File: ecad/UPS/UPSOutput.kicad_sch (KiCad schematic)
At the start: 29 parts, among them J3 USB_C_Receptacle_USB2.0_16P, Q3 IRLR7843TRPBF, SW3 SW_DPDT_x2, U2 MPQ5031GRE-0001-AEC1-P

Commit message: Swapped 201 resistor footprint
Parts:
- R40: footprint Resistor_SMD:R_0201_0603Metric_Pad0.64x0.40mm_HandSolder -> Resistor_SMD:R_0603_1608Metric_Pad0.98x0.95mm_HandSolder
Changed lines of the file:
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@@
 			)
 		)
-		(property "Footprint" "Resistor_SMD:R_0201_0603Metric_Pad0.64x0.40mm_HandSolder"
+		(property "Footprint" "Resistor_SMD:R_0603_1608Metric_Pad0.98x0.95mm_HandSolder"
 			(at 159.512 29.21 90)
 			(hide yes)

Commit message: Update R41 Resistor from 0201 to 0603
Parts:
- R41: footprint Resistor_SMD:R_0201_0603Metric_Pad0.64x0.40mm_HandSolder -> Resistor_SMD:R_0603_1608Metric_Pad0.98x0.95mm_HandSolder
- renumbered C9 to C?, C6 to C?, C10 to C?, C11 to C?, C5 to C?, C12 to C?, D4 to D?, D3 to D?, D5 to D?, D1 to D?, D2 to D?, J3 to J1, R7 to R?, R6 to R?, R8 to R?, TH1 to TH?, U2 to U1
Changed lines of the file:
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@@
 		(dnp no)
 		(fields_autoplaced yes)
-		(property "Reference" "#PWR0102"
+		(property "Reference" "#PWR03"
 			(at 66.04 33.02 0)
 			(hide yes)
@@
 		)
 		(instances
-			(project ""
+			(project "UPSOutput"
 				(path "/917f3576-2b89-40c4-9175-933056884ccc"
 					(reference "#PWR03")
@@
 		(in_pos_files yes)
 		(dnp no)
-		(property "Reference" "R7"
+		(property "Reference" "R?"
 			(at 142.24 50.292 90)
 			(show_name no)
@@
 		)
 		(instances
+			(project "UPSOutput"
+				(path "/917f3576-2b89-40c4-9175-933056884ccc"
+					(reference "TP6")
+					(unit 1)
+				)
+			)
 			(project "UPS"
 				(path "/9d92b60a-4a6b-449c-b462-cab19e69d38c/c2035c51-7de6-43a1-947f-d073f8318def"
@@
 		(in_pos_files yes)
 		(dnp no)
-		(property "Reference" "D4"
+		(property "Reference" "D?"
 			(at 195.58 76.2001 90)
 			(show_name no)
@@
 		)
 		(instances
+			(project "UPSOutput"
+				(path "/917f3576-2b89-40c4-9175-933056884ccc"
+					(reference "#PWR051")
+					(unit 1)
+				)
+			)
 			(project "UPS"
 				(path "/9d92b60a-4a6b-449c-b462-cab19e69d38c/c2035c51-7de6-43a1-947f-d073f8318def"
@@
 		(dnp no)
 		(fields_autoplaced yes)
-		(property "Reference" "#PWR09"
+		(property "Reference" "#PWR?"
 			(at 182.88 91.44 0)
 			(hide yes)
@@
 		(in_pos_files yes)
 		(dnp no)
-		(property "Reference" "D3"
+		(property "Reference" "D?"
 			(at 185.42 76.2001 90)
 			(show_name no)
@@
 		(in_pos_files yes)
 		(dnp no)
-		(property "Reference" "R6"
+		(property "Reference" "R?"
 			(at 142.24 43.688 90)
 			(show_name no)
@@
 		)
 		(instances
+			(project "UPSOutput"
+				(path "/917f3576-2b89-40c4-9175-933056884ccc"
+					(reference "C59")
+					(unit 1)
+				)
+			)
 			(project "UPS"
 				(path "/9d92b60a-4a6b-449c-b462-cab19e69d38c/c2035c51-7de6-43a1-947f-d073f8318def"
@@
 		(dnp no)
 		(fields_autoplaced yes)
-		(property "Reference" "C9"
+		(property "Reference" "C?"
 			(at 68.58 73.6599 0)
 			(show_name no)
@@
 		(in_pos_files yes)
 		(dnp no)
-		(property "Reference" "U2"
+		(property "Reference" "U1"
 			(at 92.71 74.93 0)
 			(show_name no)
@@
 		)
 		(instances
-			(project ""
+			(project "UPSOutput"
 				(path "/917f3576-2b89-40c4-9175-933056884ccc"
 					(reference "U1")
@@
 			)
 		)
-		(property "Footprint" "Resistor_SMD:R_0201_0603Metric_Pad0.64x0.40mm_HandSolder"
+		(property "Footprint" "Resistor_SMD:R_0603_1608Metric_Pad0.98x0.95mm_HandSolder"
 			(at 159.512 39.37 90)
 			(hide yes)
@@
 		)
 		(instances
+			(project "UPSOutput"
+				(path "/917f3576-2b89-40c4-9175-933056884ccc"
+					(reference "R41")
+					(unit 1)
+				)
+			)
 			(project "UPS"
 				(path "/9d92b60a-4a6b-449c-b462-cab19e69d38c/c2035c51-7de6-43a1-947f-d073f8318def"
@@
 		)
 		(instances
+			(project "UPSOutput"
+				(path "/917f3576-2b89-40c4-9175-933056884ccc"
+					(reference "C64")
+					(unit 1)
+				)
+			)
 			(project "UPS"
 				(path "/9d92b60a-4a6b-449c-b462-cab19e69d38c/c2035c51-7de6-43a1-947f-d073f8318def"
@@
 		)
 		(instances
+			(project "UPSOutput"
+				(path "/917f3576-2b89-40c4-9175-933056884ccc"
+					(reference "TP7")
+					(unit 1)
+				)
+			)
 			(project "UPS"
 				(path "/9d92b60a-4a6b-449c-b462-cab19e69d38c/c2035c51-7de6-43a1-947f-d073f8318def"
@@
 		(dnp no)
 		(fields_autoplaced yes)
-		(property "Reference" "#PWR010"
+		(property "Reference" "#PWR?"
 			(at 198.12 91.44 0)
 			(hide yes)
@@
 		(in_pos_files yes)
 		(dnp no)
-		(property "Reference" "C6"
+		(property "Reference" "C?"
 			(at 123.19 68.834 0)
 			(show_name no)
@@
 		(dnp no)
 		(fields_autoplaced yes)
-		(property "Reference" "#PWR0104"
+		(property "Reference" "#PWR01"
 			(at 243.84 21.59 0)
 			(hide yes)
@@
 		)
 		(instances
-			(project ""
+			(project "UPSOutput"
 				(path "/917f3576-2b89-40c4-9175-933056884ccc"
 					(reference "#PWR01")
@@
 		(dnp no)
 		(fields_autoplaced yes)
-		(property "Reference" "#PWR0108"
+		(property "Reference" "#PWR?"
 			(at 58.42 133.35 0)
 			(hide yes)
@@
 		(dnp no)
 		(fields_autoplaced yes)
-		(property "Reference" "#PWR011"
+		(property "Reference" "#PWR?"
 			(at 113.03 25.4 0)
 			(hide yes)
@@
 		)
 		(instances
+			(project "UPSOutput"
+				(path "/917f3576-2b89-40c4-9175-933056884ccc"
+					(reference "Q3")
+					(unit 1)
+				)
+			)
 			(project "UPS"
 				(path "/9d92b60a-4a6b-449c-b462-cab19e69d38c/c2035c51-7de6-43a1-947f-d073f8318def"
@@
 		(in_pos_files yes)
 		(dnp no)
-		(property "Reference" "C10"
+		(property "Reference" "C?"
 			(at 53.34 73.6599 0)
 			(show_name no)
@@
 		(dnp no)
 		(fields_autoplaced yes)
-		(property "Reference" "#PWR08"
+		(property "Reference" "#PWR?"
 			(at 158.75 91.44 0)
 			(hide yes)
@@
 		(dnp no)
 		(fields_autoplaced yes)
-		(property "Reference" "#PWR0117"
+		(property "Reference" "#PWR05"
 			(at 251.46 21.59 0)
 			(hide yes)
@@
 		(dnp no)
 		(fields_autoplaced yes)
-		(property "Reference" "C11"
+		(property "Reference" "C?"
 			(at 139.7 74.93 90)
 			(show_name no)
@@
 		(dnp no)
 		(fields_autoplaced yes)
-		(property "Reference" "#PWR013"
+		(property "Reference" "#PWR?"
 			(at 245.11 85.09 0)
 			(hide yes)
@@
 		(dnp no)
 		(fields_autoplaced yes)
-		(property "Reference" "#PWR0106"
+		(property "Reference" "#PWR?"
 			(at 39.37 115.57 0)
 			(hide yes)
@@
 		(in_pos_files yes)
 		(dnp no)
-		(property "Reference" "D5"
+		(property "Reference" "D?"
 			(at 232.4101 92.71 90)
 			(show_name no)
@@
 		(dnp no)
 		(fields_autoplaced yes)
-		(property "Reference" "#PWR012"
+		(property "Reference" "#PWR?"
 			(at 149.86 25.4 0)
 			(hide yes)
@@
 		(dnp no)
 		(fields_autoplaced yes)
-		(property "Reference" "#PWR0101"
+		(property "Reference" "#PWR02"
 			(at 118.11 82.55 0)
 			(hide yes)
@@
 		)
 		(instances
-			(project ""
+			(project "UPSOutput"
 				(path "/917f3576-2b89-40c4-9175-933056884ccc"
 					(reference "#PWR02")
@@
 		(dnp no)
 		(fields_autoplaced yes)
-		(property "Reference" "D1"
+		(property "Reference" "D?"
 			(at 156.21 73.6599 90)
 			(show_name no)
@@
 		)
 		(instances
+			(project "UPSOutput"
+				(path "/917f3576-2b89-40c4-9175-933056884ccc"
+					(reference "#PWR033")
+					(unit 1)
+				)
+			)
 			(project "UPS"
 				(path "/9d92b60a-4a6b-449c-b462-cab19e69d38c/c2035c51-7de6-43a1-947f-d073f8318def"
@@
 		)
 		(instances
+			(project "UPSOutput"
+				(path "/917f3576-2b89-40c4-9175-933056884ccc"
+					(reference "R35")
+					(unit 1)
+				)
+			)
 			(project "UPS"
 				(path "/9d92b60a-4a6b-449c-b462-cab19e69d38c/c2035c51-7de6-43a1-947f-d073f8318def"
@@
 		)
 		(instances
+			(project "UPSOutput"
+				(path "/917f3576-2b89-40c4-9175-933056884ccc"
+					(reference "#PWR052")
+					(unit 1)
+				)
+			)
 			(project "UPS"
 				(path "/9d92b60a-4a6b-449c-b462-cab19e69d38c/c2035c51-7de6-43a1-947f-d073f8318def"
@@
 		)
 		(instances
+			(project "UPSOutput"
+				(path "/917f3576-2b89-40c4-9175-933056884ccc"
+					(reference "F2")
+					(unit 1)
+				)
+			)
 			(project "UPS"
 				(path "/9d92b60a-4a6b-449c-b462-cab19e69d38c/c2035c51-7de6-43a1-947f-d073f8318def"
@@
 		(in_pos_files yes)
 		(dnp no)
-		(property "Reference" "D2"
+		(property "Reference" "D?"
 			(at 165.1 73.6599 90)
 			(show_name no)
@@
 		)
 		(instances
+			(project "UPSOutput"
+				(path "/917f3576-2b89-40c4-9175-933056884ccc"
+					(reference "R40")
+					(unit 1)
+				)
+			)
 			(project "UPS"
 				(path "/9d92b60a-4a6b-449c-b462-cab19e69d38c/c2035c51-7de6-43a1-947f-d073f8318def"
@@
 		(dnp no)
 		(fields_autoplaced yes)
-		(property "Reference" "C5"
+		(property "Reference" "C?"
 			(at 138.43 68.5799 0)
 			(show_name no)
@@
 		(dnp no)
 		(fields_autoplaced yes)
-		(property "Reference" "#PWR0103"
+		(property "Reference" "#PWR04"
 			(at 60.96 90.17 0)
 			(hide yes)
@@
 		)
 		(instances
+			(project "UPSOutput"
+				(path "/917f3576-2b89-40c4-9175-933056884ccc"
+					(reference "TP8")
+					(unit 1)
+				)
+			)
 			(project "UPS"
 				(path "/9d92b60a-4a6b-449c-b462-cab19e69d38c/c2035c51-7de6-43a1-947f-d073f8318def"
@@
 		)
 		(instances
+			(project "UPSOutput"
+				(path "/917f3576-2b89-40c4-9175-933056884ccc"
+					(reference "SW3")
+					(unit 1)
+				)
+			)
 			(project "UPS"
 				(path "/9d92b60a-4a6b-449c-b462-cab19e69d38c/c2035c51-7de6-43a1-947f-d073f8318def"
@@
 		(dnp no)
 		(fields_autoplaced yes)
-		(property "Reference" "R8"
+		(property "Reference" "R?"
 			(at 118.11 19.05 90)
 			(show_name no)
@@
 		(dnp no)
 		(fields_autoplaced yes)
-		(property "Reference" "#PWR0107"
+		(property "Reference" "#PWR?"
 			(at 48.26 41.91 0)
 			(hide yes)
@@
 		(dnp no)
 		(fields_autoplaced yes)
-		(property "Reference" "J3"
+		(property "Reference" "J1"
 			(at 255.27 53.3399 0)
 			(show_name no)
@@
 		)
 		(instances
-			(project ""
+			(project "UPSOutput"
 				(path "/917f3576-2b89-40c4-9175-933056884ccc"
 					(reference "J1")
@@
 		(in_pos_files yes)
 		(dnp no)
-		(property "Reference" "TH1"
+		(property "Reference" "TH?"
 			(at 133.6675 19.05 90)
 			(show_name no)
@@
 		)
 		(instances
+			(project "UPSOutput"
+				(path "/917f3576-2b89-40c4-9175-933056884ccc"
+					(reference "C60")
+					(unit 1)
+				)
+			)
 			(project "UPS"
 				(path "/9d92b60a-4a6b-449c-b462-cab19e69d38c/c2035c51-7de6-43a1-947f-d073f8318def"
@@
 		(dnp no)
 		(fields_autoplaced yes)
-		(property "Reference" "C12"
+		(property "Reference" "C?"
 			(at 231.14 77.47 90)
 			(show_name no)
@@
 		)
 	)
+	(embedded_fonts no)
 )

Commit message: Light PCB work
Also removed NetTie
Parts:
- gave numbers to parts that had none: 15
- renumbered J1 to J3, U1 to U2
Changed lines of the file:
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@@
 		(dnp no)
 		(fields_autoplaced yes)
-		(property "Reference" "#PWR03"
+		(property "Reference" "#PWR0102"
 			(at 66.04 33.02 0)
 			(hide yes)
@@
 		(in_pos_files yes)
 		(dnp no)
-		(property "Reference" "R?"
+		(property "Reference" "R7"
 			(at 142.24 50.292 90)
 			(show_name no)
@@
 		(in_pos_files yes)
 		(dnp no)
-		(property "Reference" "D?"
+		(property "Reference" "D4"
 			(at 195.58 76.2001 90)
 			(show_name no)
@@
 		(dnp no)
 		(fields_autoplaced yes)
-		(property "Reference" "#PWR?"
+		(property "Reference" "#PWR09"
 			(at 182.88 91.44 0)
 			(hide yes)
@@
 		(in_pos_files yes)
 		(dnp no)
-		(property "Reference" "D?"
+		(property "Reference" "D3"
 			(at 185.42 76.2001 90)
 			(show_name no)
@@
 		(in_pos_files yes)
 		(dnp no)
-		(property "Reference" "R?"
+		(property "Reference" "R6"
 			(at 142.24 43.688 90)
 			(show_name no)
@@
 		(dnp no)
 		(fields_autoplaced yes)
-		(property "Reference" "C?"
+		(property "Reference" "C9"
 			(at 68.58 73.6599 0)
 			(show_name no)
@@
 		(in_pos_files yes)
 		(dnp no)
-		(property "Reference" "U1"
+		(property "Reference" "U2"
 			(at 92.71 74.93 0)
 			(show_name no)
@@
 		(dnp no)
 		(fields_autoplaced yes)
-		(property "Reference" "#PWR?"
+		(property "Reference" "#PWR010"
 			(at 198.12 91.44 0)
 			(hide yes)
@@
 		(in_pos_files yes)
 		(dnp no)
-		(property "Reference" "C?"
+		(property "Reference" "C6"
 			(at 123.19 68.834 0)
 			(show_name no)
@@
 		(dnp no)
 		(fields_autoplaced yes)
-		(property "Reference" "#PWR01"
+		(property "Reference" "#PWR0104"
 			(at 243.84 21.59 0)
 			(hide yes)
@@
 		(dnp no)
 		(fields_autoplaced yes)
-		(property "Reference" "#PWR?"
+		(property "Reference" "#PWR0108"
 			(at 58.42 133.35 0)
 			(hide yes)
@@
 		(dnp no)
 		(fields_autoplaced yes)
-		(property "Reference" "#PWR?"
+		(property "Reference" "#PWR011"
 			(at 113.03 25.4 0)
 			(hide yes)
@@
 		(in_pos_files yes)
 		(dnp no)
-		(property "Reference" "C?"
+		(property "Reference" "C10"
 			(at 53.34 73.6599 0)
 			(show_name no)
@@
 		(dnp no)
 		(fields_autoplaced yes)
-		(property "Reference" "#PWR?"
+		(property "Reference" "#PWR08"
 			(at 158.75 91.44 0)
 			(hide yes)
@@
 		(dnp no)
 		(fields_autoplaced yes)
-		(property "Reference" "#PWR05"
+		(property "Reference" "#PWR0117"
 			(at 251.46 21.59 0)
 			(hide yes)
@@
 		(dnp no)
 		(fields_autoplaced yes)
-		(property "Reference" "C?"
+		(property "Reference" "C11"
 			(at 139.7 74.93 90)
 			(show_name no)
@@
 		(dnp no)
 		(fields_autoplaced yes)
-		(property "Reference" "#PWR?"
+		(property "Reference" "#PWR013"
 			(at 245.11 85.09 0)
 			(hide yes)
@@
 		(dnp no)
 		(fields_autoplaced yes)
-		(property "Reference" "#PWR?"
+		(property "Reference" "#PWR0106"
 			(at 39.37 115.57 0)
 			(hide yes)
@@
 		(in_pos_files yes)
 		(dnp no)
-		(property "Reference" "D?"
+		(property "Reference" "D5"
 			(at 232.4101 92.71 90)
 			(show_name no)
@@
 		(dnp no)
 		(fields_autoplaced yes)
-		(property "Reference" "#PWR?"
+		(property "Reference" "#PWR012"
 			(at 149.86 25.4 0)
 			(hide yes)
@@
 		(dnp no)
 		(fields_autoplaced yes)
-		(property "Reference" "#PWR02"
+		(property "Reference" "#PWR0101"
 			(at 118.11 82.55 0)
 			(hide yes)
@@
 		(dnp no)
 		(fields_autoplaced yes)
-		(property "Reference" "D?"
+		(property "Reference" "D1"
 			(at 156.21 73.6599 90)
 			(show_name no)
@@
 		(in_pos_files yes)
 		(dnp no)
-		(property "Reference" "D?"
+		(property "Reference" "D2"
 			(at 165.1 73.6599 90)
 			(show_name no)
@@
 		(dnp no)
 		(fields_autoplaced yes)
-		(property "Reference" "C?"
+		(property "Reference" "C5"
 			(at 138.43 68.5799 0)
 			(show_name no)
@@
 		(dnp no)
 		(fields_autoplaced yes)
-		(property "Reference" "#PWR04"
+		(property "Reference" "#PWR0103"
 			(at 60.96 90.17 0)
 			(hide yes)
@@
 		(dnp no)
 		(fields_autoplaced yes)
-		(property "Reference" "R?"
+		(property "Reference" "R8"
 			(at 118.11 19.05 90)
 			(show_name no)
@@
 		(dnp no)
 		(fields_autoplaced yes)
-		(property "Reference" "#PWR?"
+		(property "Reference" "#PWR0107"
 			(at 48.26 41.91 0)
 			(hide yes)
@@
 		(dnp no)
 		(fields_autoplaced yes)
-		(property "Reference" "J1"
+		(property "Reference" "J3"
 			(at 255.27 53.3399 0)
 			(show_name no)
@@
 		(in_pos_files yes)
 		(dnp no)
-		(property "Reference" "TH?"
+		(property "Reference" "TH1"
 			(at 133.6675 19.05 90)
 			(show_name no)
@@
 		(dnp no)
 		(fields_autoplaced yes)
-		(property "Reference" "C?"
+		(property "Reference" "C12"
 			(at 231.14 77.47 90)
 			(show_name no)
@@
 		)
 	)
-	(embedded_fonts no)
 )

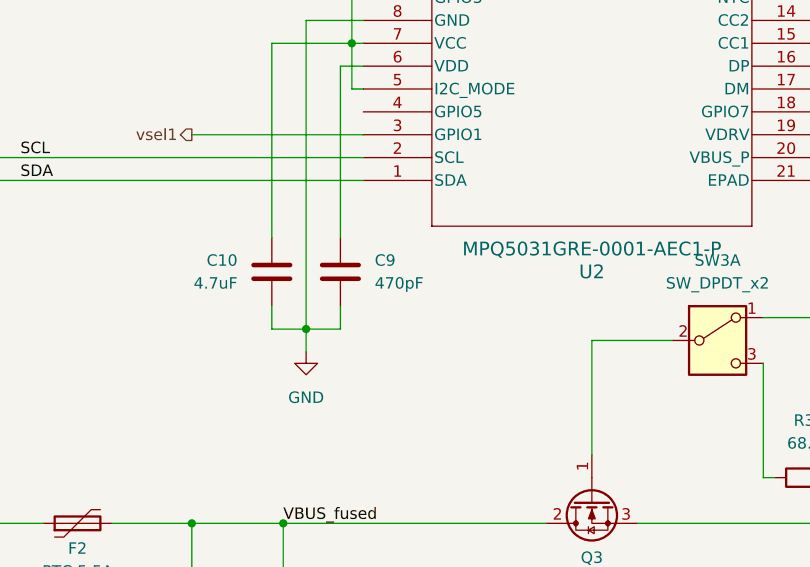
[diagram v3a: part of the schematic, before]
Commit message: eh
Grounded the charger’s cell-count divider.
Corrected C9 from 470 pF to 470 nF.
Connected the STM’s unused LCD supply pin.
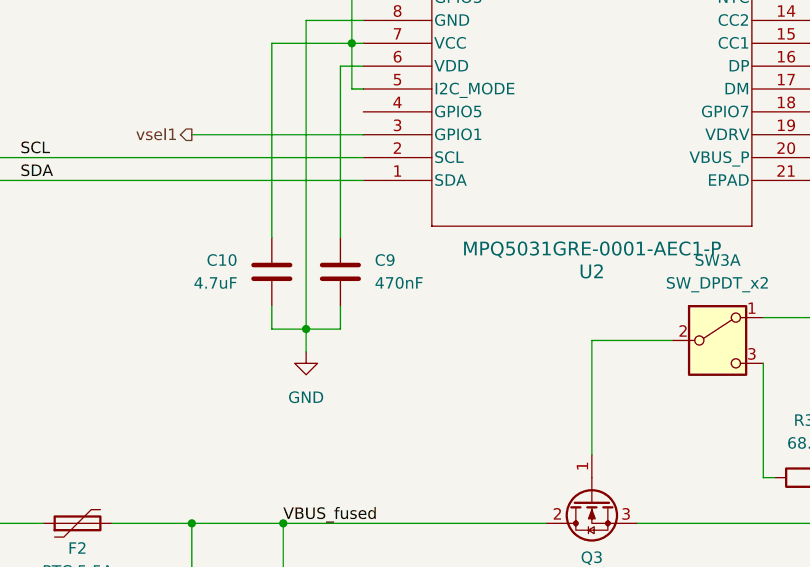
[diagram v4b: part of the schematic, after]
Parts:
- C9: value 470pF -> 470nF
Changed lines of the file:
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@@
 			)
 		)
-		(property "Value" "470pF"
+		(property "Value" "470nF"
 			(at 68.58 76.1999 0)
 			(show_name no)
